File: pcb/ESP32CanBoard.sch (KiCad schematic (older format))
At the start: 39 parts, among them IC101 SP3481CN, K1 1Wire, P101 CAN, P102 RS485, P103 Display, P104 Dsiplay, P3 CONN_1, P4 CONN_1, P5 CONN_1, P6 CONN_1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

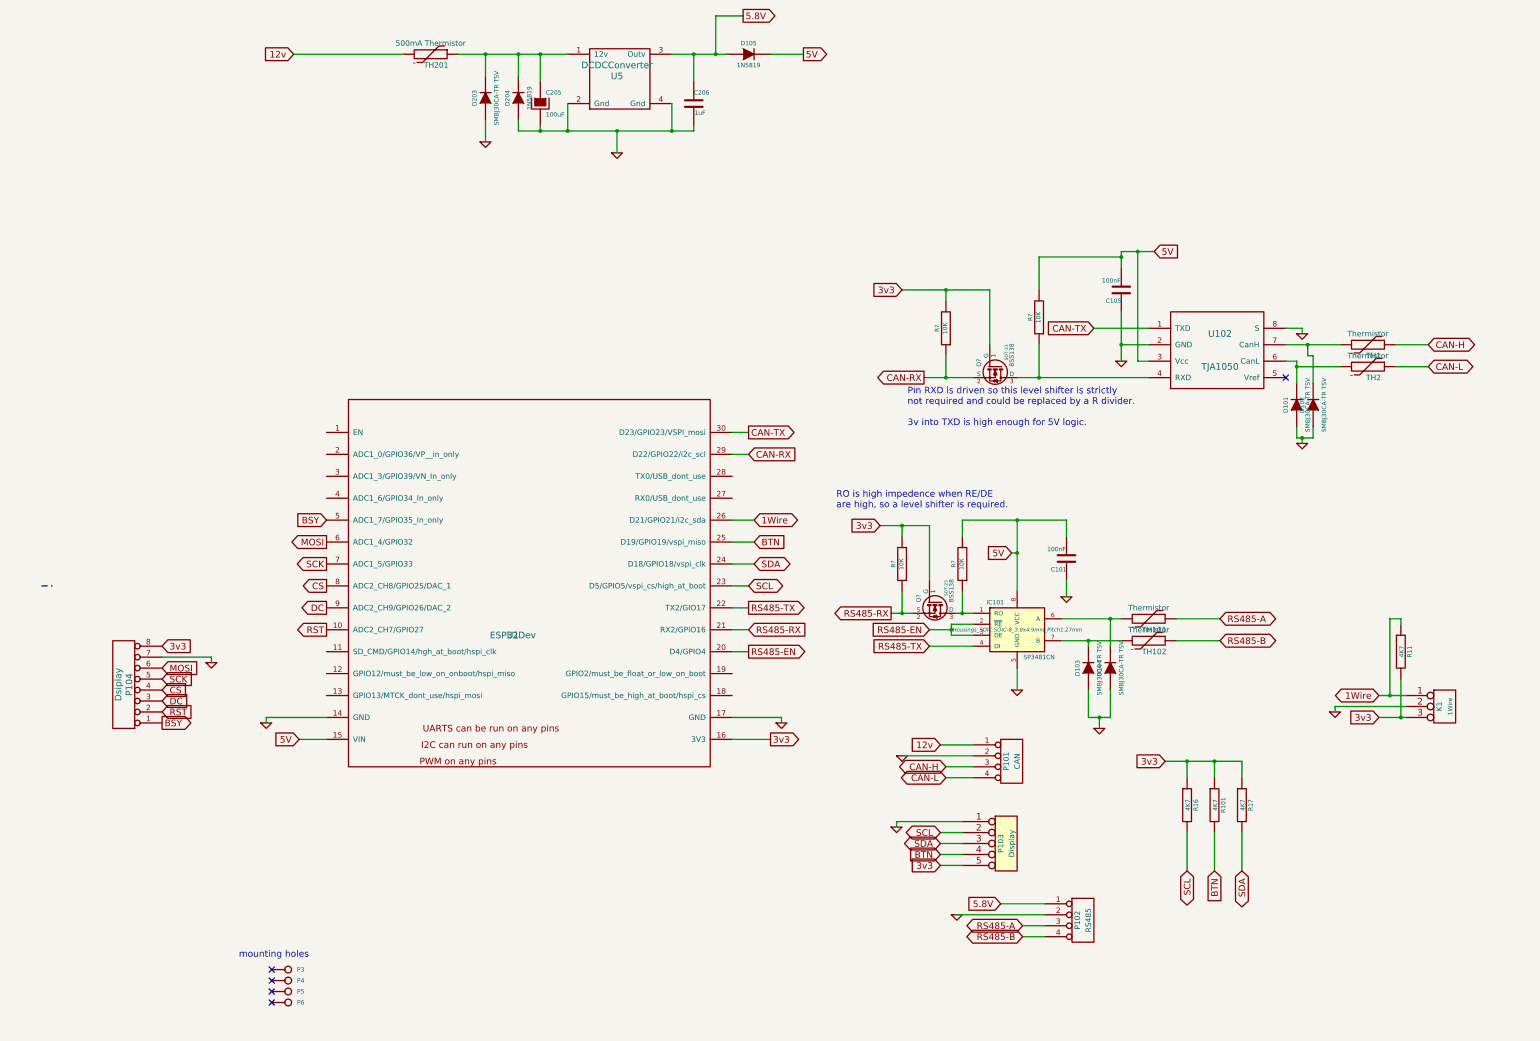
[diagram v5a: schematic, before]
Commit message: Added TFT display module, and made Modbusmaster non blocking
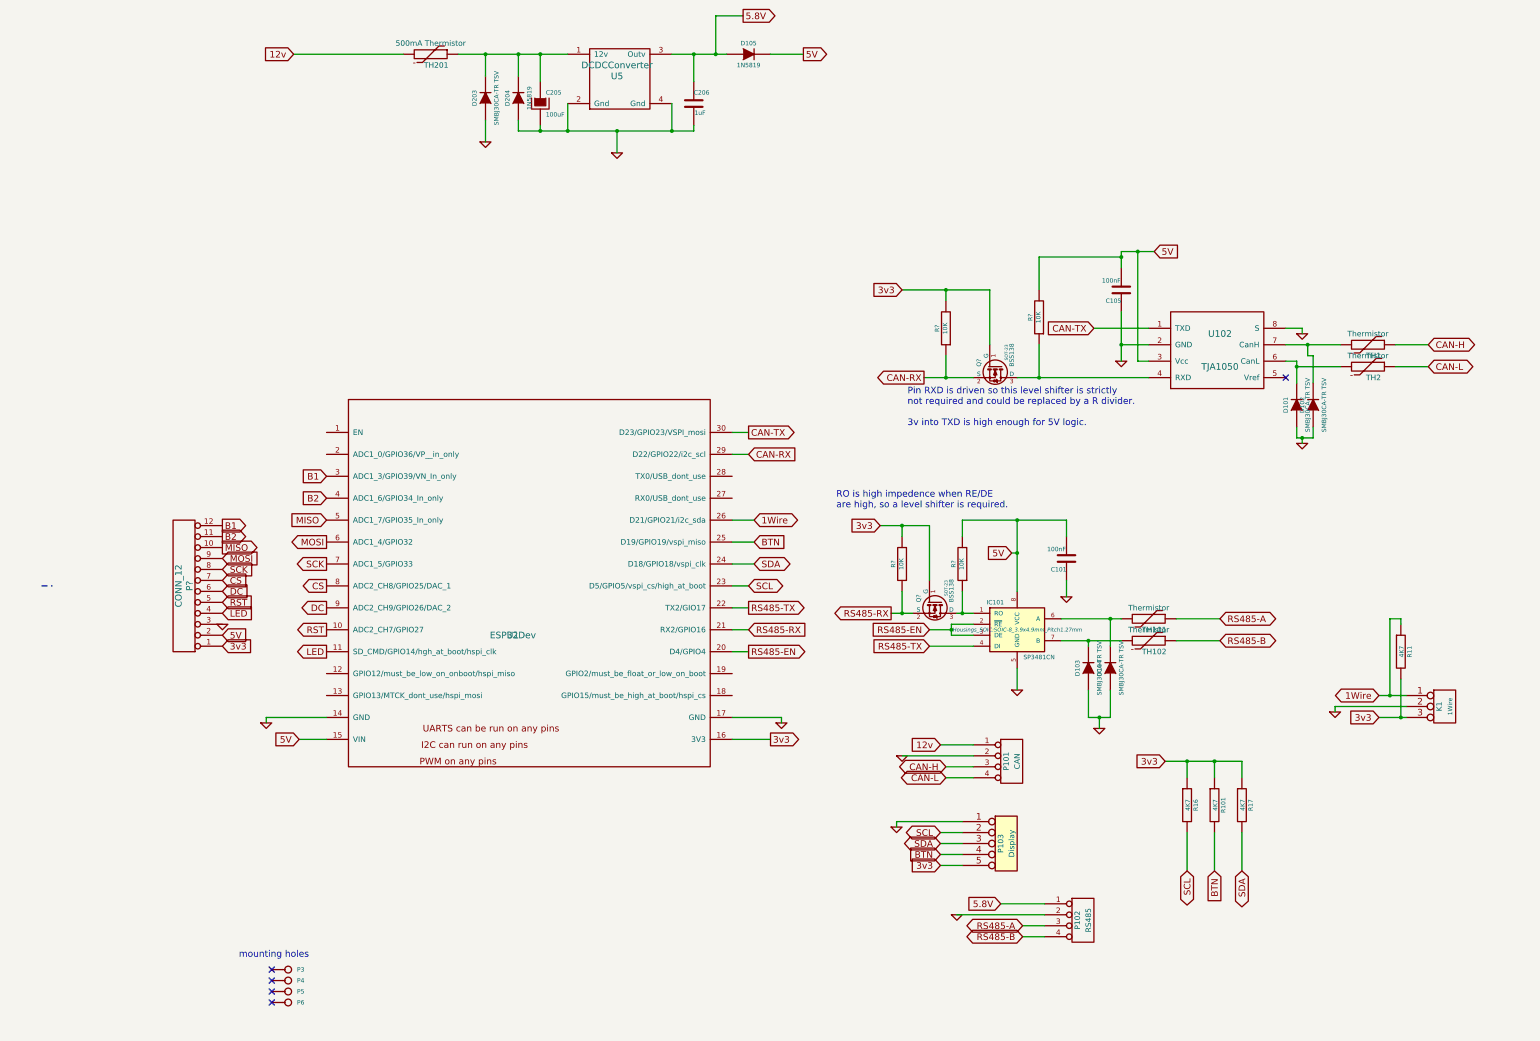
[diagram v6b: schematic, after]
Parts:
- removed P104: Dsiplay, Pin_Headers:Pin_Header_Straight_1x08, symbol CONN_8
- added P?: CONN_12, symbol CONN_12
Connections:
- net 3v3: now also P?.1 (P1)
- net 5V: now also P?.2 (P2)
- net CS: now also P?.7 (P7)
- net DC: now also P?.6 (P6)
- net GND: now also P?.3 (P3)
- net MOSI: now also P?.9 (P9)
- net RST: now also P?.5 (P5)
- net SCK: now also P?.8 (P8)
- net LED: now reaches U1.11 (SD_CMD/GPIO14/hgh_at_boot/hspi_clk)
- net LED: now also P?.4 (P4)
- net B1: now reaches U1.3 (ADC1_3/GPIO39/VN_In_only)
- net B1: now also P?.12 (P12)
- net B2: now reaches U1.4 (ADC1_6/GPIO34_In_only)
- net B2: now also P?.11 (P11)
- net BSY renamed MISO
- net MISO: now also P?.10 (P10)
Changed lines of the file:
@@
 	3100 1150 4100 1150
 Wire Wire Line
-	4600 1150 5600 1150
+	4600 1150 4850 1150
+Wire Wire Line
+	4850 1150 5150 1150
+Wire Wire Line
+	5150 1150 5350 1150
+Wire Wire Line
+	5350 1150 5600 1150
 Wire Wire Line
 	5350 1150 5350 1400
 Connection ~ 5350 1150
 Wire Wire Line
-	5150 1850 6750 1850
+	5150 1850 5350 1850
+Wire Wire Line
+	5350 1850 5600 1850
+Wire Wire Line
+	5600 1850 6050 1850
+Wire Wire Line
+	6050 1850 6550 1850
+Wire Wire Line
+	6550 1850 6750 1850
 Wire Wire Line
 	6750 1850 6750 1800
@@
 Connection ~ 6050 1850
 Wire Wire Line
-	6550 1150 7050 1150
+	6550 1150 6750 1150
+Wire Wire Line
+	6750 1150 6950 1150
+Wire Wire Line
+	6950 1150 7050 1150
 Wire Wire Line
 	6750 1150 6750 1400
@@
 $EndComp
 Wire Wire Line
-	12150 3800 12650 3800
+	12150 3800 12350 3800
+Wire Wire Line
+	12350 3800 12650 3800
 Wire Wire Line
 	12250 4000 12650 4000
 Wire Wire Line
-	12250 3950 12250 4150
+	12250 3950 12250 4000
+Wire Wire Line
+	12250 4000 12250 4150
 Wire Wire Line
 	12250 3950 12150 3950
@@
 	12250 4550 12250 4650
 Wire Wire Line
-	12250 4650 12400 4650
+	12250 4650 12300 4650
+Wire Wire Line
+	12300 4650 12400 4650
 Wire Wire Line
 	12400 4650 12400 4550
@@
 $EndComp
 Wire Wire Line
-	10650 3500 10650 3950
+	10650 3500 10650 3800
+Wire Wire Line
+	10650 3800 10650 3950
 Connection ~ 10650 3800
 Wire Wire Line
-	10650 2950 10650 3100
-Wire Wire Line
-	10650 2950 10950 2950
+	10650 2950 10650 3000
+Wire Wire Line
+	10650 3000 10650 3100
+Wire Wire Line
+	10650 2950 10800 2950
+Wire Wire Line
+	10800 2950 10950 2950
 Wire Wire Line
 	10800 2950 10800 3950
@@
 	13100 6300 13100 7000
 Wire Wire Line
-	13000 7000 13250 7000
+	13000 7000 13100 7000
+Wire Wire Line
+	13100 7000 13250 7000
 Connection ~ 13100 7000
 Wire Wire Line
-	13000 7200 13250 7200
+	13000 7200 13200 7200
+Wire Wire Line
+	13200 7200 13250 7200
 $Comp
 L DCDCConverter U5
@@
 3v3
 Wire Wire Line
-	11050 7600 11750 7600
+	11050 7600 11250 7600
+Wire Wire Line
+	11250 7600 11500 7600
+Wire Wire Line
+	11500 7600 11750 7600
 Wire Wire Line
 	11750 7600 11750 7750
@@
 $EndComp
 Wire Wire Line
-	10100 6300 10650 6300
+	10100 6300 10550 6300
+Wire Wire Line
+	10550 6300 10650 6300
 Wire Wire Line
 	11150 6300 11550 6300
@@
 	11150 6500 11550 6500
 Wire Wire Line
-	10100 6500 10650 6500
+	10100 6500 10350 6500
+Wire Wire Line
+	10350 6500 10650 6500
 Wire Wire Line
 	10550 6550 10550 6300
@@
 	10350 6950 10350 7200
 Wire Wire Line
-	10350 7200 10550 7200
+	10350 7200 10450 7200
+Wire Wire Line
+	10450 7200 10550 7200
 Wire Wire Line
 	10550 7200 10550 6950
@@
 	9650 5700 9700 5700
 Wire Wire Line
-	9700 5400 9700 6050
+	9700 5400 9700 5700
+Wire Wire Line
+	9700 5700 9700 6050
 Wire Wire Line
 	9300 6350 9100 6350
 Wire Wire Line
-	9100 6350 9100 6450
+	9100 6350 9100 6400
+Wire Wire Line
+	9100 6400 9100 6450
 Wire Wire Line
 	9100 6450 9300 6450
@@
 $EndComp
 Wire Wire Line
-	9200 5400 10150 5400
+	9200 5400 9700 5400
+Wire Wire Line
+	9700 5400 10150 5400
 Wire Wire Line
 	10150 5400 10150 5550
@@
 Text GLabel 3400 6000 0    60   Output ~ 0
 CS
-Text GLabel 1900 6750 2    60   Input ~ 0
-MOSI
-Text GLabel 1900 6850 2    60   Input ~ 0
-SCK
-Text GLabel 1900 6950 2    60   Input ~ 0
-CS
-$Comp
-L CONN_8 P104
-U 1 1 62C19D21
-P 1550 6900
-F 0 "P104" V 1500 6900 60  0000 C CNN
-F 1 "Dsiplay" V 1600 6900 60  0000 C CNN
-F 2 "Pin_Headers:Pin_Header_Straight_1x08" H 1550 6900 60  0001 C CNN
-F 3 "" H 1550 6900 60  0001 C CNN
-	1    1550 6900
-	-1   0    0    1
-$EndComp
-Text GLabel 1900 6550 2    60   Input ~ 0
-3v3
-$Comp
-L GND #PWR016
-U 1 1 62C1A102
-P 2350 6700
-F 0 "#PWR016" H 2350 6700 30  0001 C CNN
-F 1 "GND" H 2350 6630 30  0001 C CNN
-F 2 "" H 2350 6700 60  0001 C CNN
-F 3 "" H 2350 6700 60  0001 C CNN
-	1    2350 6700
-	1    0    0    -1
-$EndComp
-Text GLabel 1900 7050 2    60   Input ~ 0
-DC
-Text GLabel 1900 7150 2    60   Input ~ 0
-RST
-Wire Wire Line
-	1900 6650 2350 6650
-Wire Wire Line
-	2350 6650 2350 6700
-Text GLabel 1900 7250 2    60   Output ~ 0
-BSY
 Text GLabel 3400 5400 0    60   Input ~ 0
-BSY
+MISO
 Text GLabel 3400 6200 0    60   Output ~ 0
 DC
@@
 $EndComp
 Wire Wire Line
-	8850 4100 9300 4100
+	8850 4100 9050 4100
+Wire Wire Line
+	9050 4100 9300 4100
 Wire Wire Line
 	9050 3900 9050 4100
@@
 	9450 3300 9450 3800
 Wire Wire Line
-	8650 3300 9450 3300
+	8650 3300 9050 3300
+Wire Wire Line
+	9050 3300 9450 3300
 Wire Wire Line
 	9050 3300 9050 3400
 Wire Wire Line
-	9700 4100 10900 4100
+	9700 4100 9900 4100
+Wire Wire Line
+	9900 4100 10900 4100
 Wire Wire Line
 	9900 3800 9900 4100
@@
 $EndComp
 Wire Wire Line
-	9150 6250 9300 6250
-Wire Wire Line
-	8550 6250 8750 6250
+	9150 6250 9200 6250
+Wire Wire Line
+	9200 6250 9300 6250
+Wire Wire Line
+	8550 6250 8650 6250
+Wire Wire Line
+	8650 6250 8750 6250
 Text GLabel 8650 3300 0    60   Input ~ 0
 3v3
@@
 	8650 5550 8650 5450
 Wire Wire Line
-	8450 5450 8900 5450
+	8450 5450 8650 5450
+Wire Wire Line
+	8650 5450 8900 5450
 Wire Wire Line
 	8900 5450 8900 5950
@@
 Text Notes 8700 4550 0    60   ~ 0
 Pin RXD is driven so this level shifter is strictly \nnot required and could be replaced by a R divider.\n\n3v into TXD is high enough for 5V logic.\n
+Text GLabel 3400 6600 0    60   Output ~ 0
+LED
+$Comp
+L CONN_12 P?
+U 1 1 63CF9FAE
+P 2100 6000
+F 0 "P?" V 2050 6000 60  0000 C CNN
+F 1 "CONN_12" V 2150 6000 60  0000 C CNN
+F 2 "" H 2100 6000 60  0001 C CNN
+F 3 "" H 2100 6000 60  0001 C CNN
+	1    2100 6000
+	-1   0    0    1
+$EndComp
+Text GLabel 2450 6550 2    60   Input ~ 0
+3v3
+$Comp
+L GND #PWR?
+U 1 1 63CFA138
+P 2450 6350
+F 0 "#PWR?" H 2450 6350 30  0001 C CNN
+F 1 "GND" H 2450 6280 30  0001 C CNN
+F 2 "" H 2450 6350 60  0001 C CNN
+F 3 "" H 2450 6350 60  0001 C CNN
+	1    2450 6350
+	1    0    0    -1
+$EndComp
+Text GLabel 2450 6450 2    60   Input ~ 0
+5V
+Text GLabel 2450 5750 2    60   Input ~ 0
+MOSI
+Text GLabel 2450 5650 2    60   Output ~ 0
+MISO
+Text GLabel 2450 5850 2    60   Input ~ 0
+SCK
+Text GLabel 2450 5950 2    60   Input ~ 0
+CS
+Text GLabel 2450 6050 2    60   Input ~ 0
+DC
+Text GLabel 2450 6150 2    60   Input ~ 0
+RST
+Text GLabel 2450 6250 2    60   Input ~ 0
+LED
+Text GLabel 2450 5450 2    60   Output ~ 0
+B1
+Text GLabel 2450 5550 2    60   Output ~ 0
+B2
+Text GLabel 3400 5000 0    60   Input ~ 0
+B1
+Text GLabel 3400 5200 0    60   Input ~ 0
+B2
 $EndSCHEMATC

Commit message: Added polar calculations for display
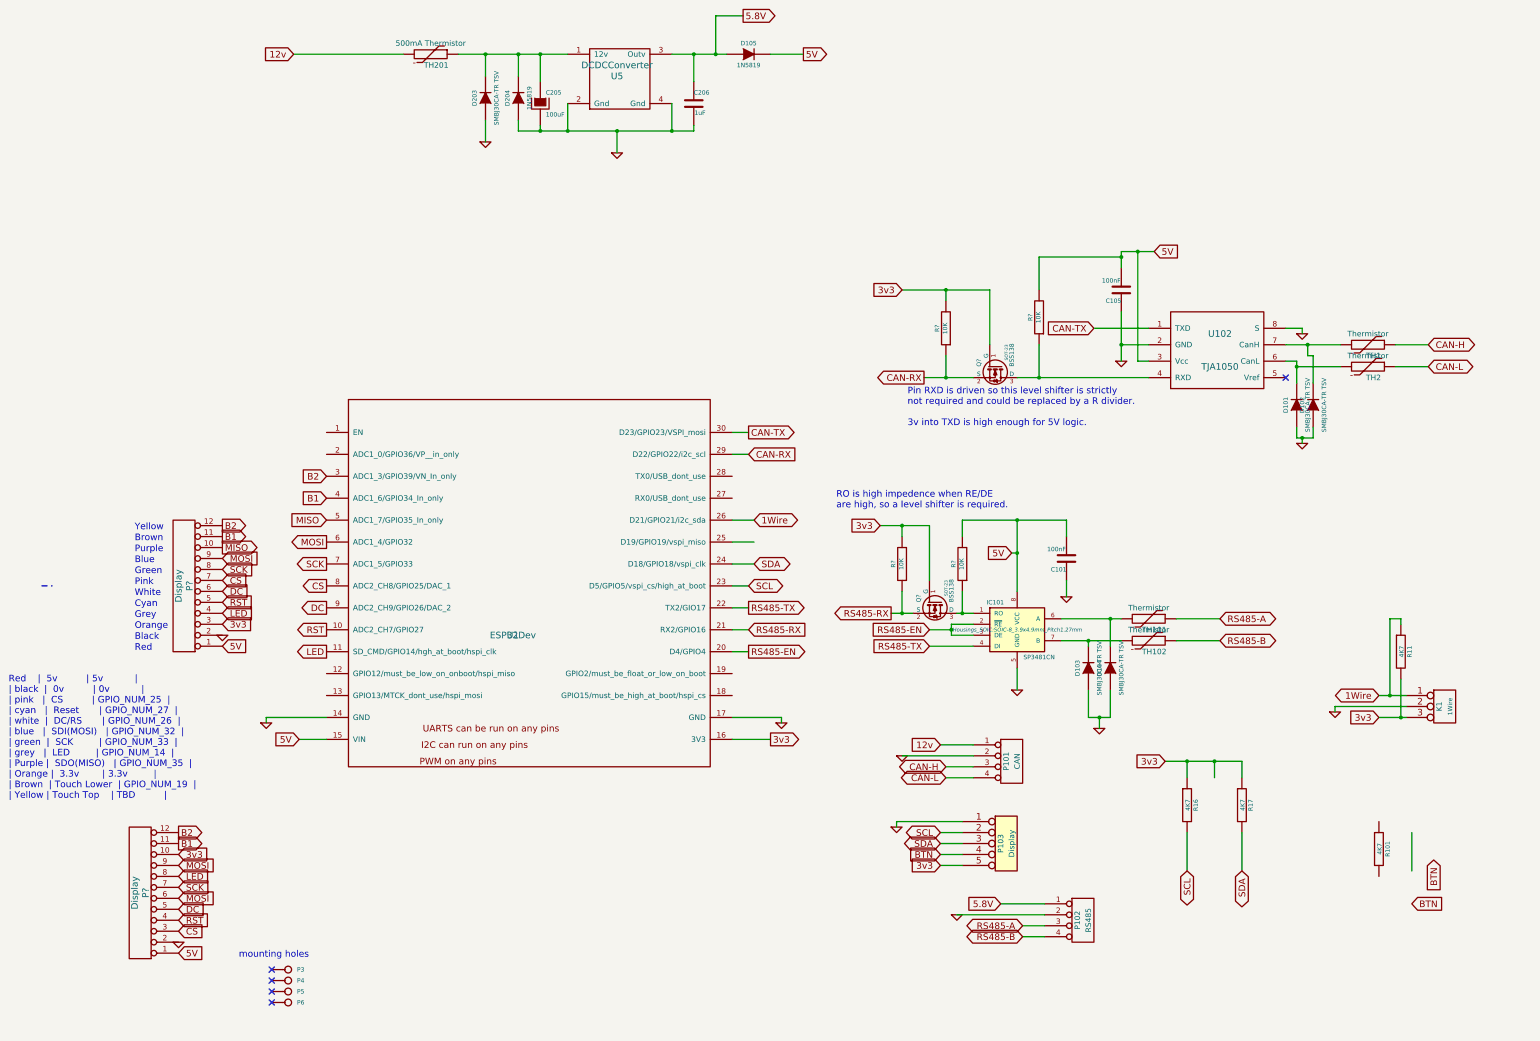
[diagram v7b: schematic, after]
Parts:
- added P?: Display, symbol CONN_12
- P?: value CONN_12 -> Display
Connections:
- net 3v3: now also P?.3 (P3), P?.10 (P10); no longer P?.1 (P1), R101.1
- net 5V: now also P?.1 (P1), P?.1 (P1); no longer P?.2 (P2)
- net B1: now also P?.11 (P11), U1.4 (ADC1_6/GPIO34_In_only), P?.11 (P11); no longer P?.12 (P12), U1.3 (ADC1_3/GPIO39/VN_In_only)
- net B2: now also P?.12 (P12), U1.3 (ADC1_3/GPIO39/VN_In_only), P?.12 (P12); no longer P?.11 (P11), U1.4 (ADC1_6/GPIO34_In_only)
- net BTN: no longer R101.2, U1.25 (D19/GPIO19/vspi_miso)
- net CS: now also P?.3 (P3)
- net DC: now also P?.5 (P5)
- net GND: now also P?.2 (P2), P?.2 (P2); no longer P?.3 (P3)
- net LED: now also P?.8 (P8)
- net MOSI: now also P?.6 (P6), P?.9 (P9)
- net RST: now also P?.4 (P4)
- net SCK: now also P?.7 (P7)
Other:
- note added: "Black"
- note added: "Blue"
- note added: "Brown"
- note added: "Cyan"
- note added: "Green"
- note added: "Grey"
- note added: "Orange"
- note added: "Pink"
- note added: "Purple"
- note added: "Red"
- note added: "Red | 5v | 5v |\n| black | 0v | 0v |\n| pink | CS | GPIO_NUM_25 |\n| cyan | Reset | GPIO_NUM_27 |\n| white | DC/RS | GPIO_NUM_26 |\n| blue | SDI(MOSI) | GPIO_NUM_32 |\n| green | SCK | GPIO_NUM_33 |\n| grey | LED | GPIO_NUM_14 |\n| Purple | SDO(MISO) | GPIO_NUM_35 |\n| Orange | 3.3v | 3.3v |\n| Brown | Touch Lower | GPIO_NUM_19 |\n| Yellow | Touch Top | TBD |"
- note added: "White"
- note added: "Yellow"
- moved on the sheet: R101
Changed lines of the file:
@@
 	1    0    0    -1
 $EndComp
-Text GLabel 7300 5600 2    60   Input ~ 0
+Text GLabel 13300 8900 2    60   Input ~ 0
 BTN
 Text GLabel 9000 8250 0    60   BiDi ~ 0
@@
 L R R101
 U 1 1 62C15F60
-P 11500 8000
-F 0 "R101" V 11580 8000 40  0000 C CNN
-F 1 "4K7" V 11507 8001 40  0000 C CNN
-F 2 "Resistors_SMD:R_0805" V 11430 8000 30  0001 C CNN
-F 3 "" H 11500 8000 30  0000 C CNN
-	1    11500 8000
+P 13000 8400
+F 0 "R101" V 13080 8400 40  0000 C CNN
+F 1 "4K7" V 13007 8401 40  0000 C CNN
+F 2 "Resistors_SMD:R_0805" V 12930 8400 30  0001 C CNN
+F 3 "" H 13000 8400 30  0000 C CNN
+	1    13000 8400
 	1    0    0    -1
 $EndComp
@@
 	11500 7750 11500 7600
 Connection ~ 11500 7600
-Text GLabel 11500 8600 3    60   Input ~ 0
+Text GLabel 13500 8500 3    60   Input ~ 0
 BTN
 Wire Wire Line
-	11500 8250 11500 8600
+	13300 8250 13300 8600
 Wire Wire Line
 	9000 8450 9200 8450
@@
 P 2100 6000
 F 0 "P?" V 2050 6000 60  0000 C CNN
-F 1 "CONN_12" V 2150 6000 60  0000 C CNN
+F 1 "Display" V 2150 6000 60  0000 C CNN
 F 2 "" H 2100 6000 60  0001 C CNN
 F 3 "" H 2100 6000 60  0001 C CNN
@@
 	-1   0    0    1
 $EndComp
-Text GLabel 2450 6550 2    60   Input ~ 0
+Text GLabel 2450 6350 2    60   Input ~ 0
 3v3
 $Comp
 L GND #PWR?
 U 1 1 63CFA138
-P 2450 6350
-F 0 "#PWR?" H 2450 6350 30  0001 C CNN
-F 1 "GND" H 2450 6280 30  0001 C CNN
-F 2 "" H 2450 6350 60  0001 C CNN
-F 3 "" H 2450 6350 60  0001 C CNN
-	1    2450 6350
-	1    0    0    -1
-$EndComp
-Text GLabel 2450 6450 2    60   Input ~ 0
+P 2450 6450
+F 0 "#PWR?" H 2450 6450 30  0001 C CNN
+F 1 "GND" H 2450 6380 30  0001 C CNN
+F 2 "" H 2450 6450 60  0001 C CNN
+F 3 "" H 2450 6450 60  0001 C CNN
+	1    2450 6450
+	1    0    0    -1
+$EndComp
+Text GLabel 2450 6550 2    60   Input ~ 0
 5V
 Text GLabel 2450 5750 2    60   Input ~ 0
@@
 Text GLabel 2450 6250 2    60   Input ~ 0
 LED
+Text GLabel 2450 5550 2    60   Output ~ 0
+B1
 Text GLabel 2450 5450 2    60   Output ~ 0
+B2
+Text GLabel 3400 5200 0    60   Input ~ 0
 B1
-Text GLabel 2450 5550 2    60   Output ~ 0
+Text GLabel 3400 5000 0    60   Input ~ 0
 B2
-Text GLabel 3400 5000 0    60   Input ~ 0
+Text Notes 1650 6400 0    60   ~ 0
+Orange
+Text Notes 1650 6600 0    60   ~ 0
+Red
+Text Notes 1650 6500 0    60   ~ 0
+Black
+Text Notes 500  7950 0    60   ~ 0
+ Red    |  5v          | 5v           |\n| black  |  0v          | 0v           |\n| pink   |  CS          | GPIO_NUM_25  |\n| cyan   |  Reset       | GPIO_NUM_27  |\n| white  |  DC/RS       | GPIO_NUM_26  |\n| blue   |  SDI(MOSI)   | GPIO_NUM_32  |\n| green  |  SCK         | GPIO_NUM_33  |\n| grey   |  LED         | GPIO_NUM_14  |\n| Purple |  SDO(MISO)   | GPIO_NUM_35  |\n| Orange |  3.3v        | 3.3v         |\n| Brown  | Touch Lower  | GPIO_NUM_19  |\n| Yellow | Touch Top    | TBD          |
+Text Notes 1650 6000 0    60   ~ 0
+Pink
+Text Notes 1650 6200 0    60   ~ 0
+Cyan
+Text Notes 1650 6100 0    60   ~ 0
+White
+Text Notes 1650 5800 0    60   ~ 0
+Blue
+Text Notes 1650 5900 0    60   ~ 0
+Green
+Text Notes 1650 6300 0    60   ~ 0
+Grey
+Text Notes 1650 5700 0    60   ~ 0
+Purple
+Text Notes 1650 5600 0    60   ~ 0
+Brown
+Text Notes 1650 5500 0    60   ~ 0
+Yellow
+$Comp
+L CONN_12 P?
+U 1 1 64180578
+P 1700 8800
+F 0 "P?" V 1650 8800 60  0000 C CNN
+F 1 "Display" V 1750 8800 60  0000 C CNN
+F 2 "" H 1700 8800 60  0001 C CNN
+F 3 "" H 1700 8800 60  0001 C CNN
+	1    1700 8800
+	-1   0    0    1
+$EndComp
+Text GLabel 2050 9350 2    60   Input ~ 0
+5V
+$Comp
+L GND #PWR?
+U 1 1 641806B2
+P 2050 9250
+F 0 "#PWR?" H 2050 9250 30  0001 C CNN
+F 1 "GND" H 2050 9180 30  0001 C CNN
+F 2 "" H 2050 9250 60  0001 C CNN
+F 3 "" H 2050 9250 60  0001 C CNN
+	1    2050 9250
+	1    0    0    -1
+$EndComp
+Text GLabel 2050 9150 2    60   Input ~ 0
+CS
+Text GLabel 2050 9050 2    60   Input ~ 0
+RST
+Text GLabel 2050 8950 2    60   Input ~ 0
+DC
+Text GLabel 2050 8850 2    60   Input ~ 0
+MOSI
+Text GLabel 2050 8750 2    60   Input ~ 0
+SCK
+Text GLabel 2050 8650 2    60   Input ~ 0
+LED
+Text GLabel 2050 8550 2    60   Input ~ 0
+MOSI
+Text GLabel 2050 8450 2    60   Input ~ 0
+3v3
+Text GLabel 2050 8350 2    60   Output ~ 0
 B1
-Text GLabel 3400 5200 0    60   Input ~ 0
+Text GLabel 2050 8250 2    60   Output ~ 0
 B2
 $EndSCHEMATC
